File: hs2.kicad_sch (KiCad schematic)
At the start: 87 parts, among them J1 Conn_01x01, J2 Conn_01x01, J3 Conn_01x02, Q1 2N5457, Q2 2N3904, Q3 2N3906, Q4 2N3904, U1 Opamp_Dual, U2 Opamp_Dual, U3 Opamp_Dual

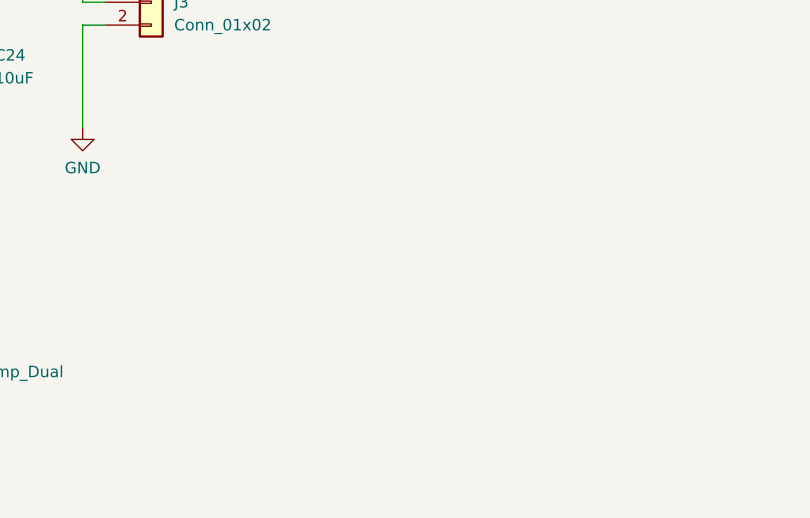
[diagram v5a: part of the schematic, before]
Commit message: schematics: Fixing ERC errors
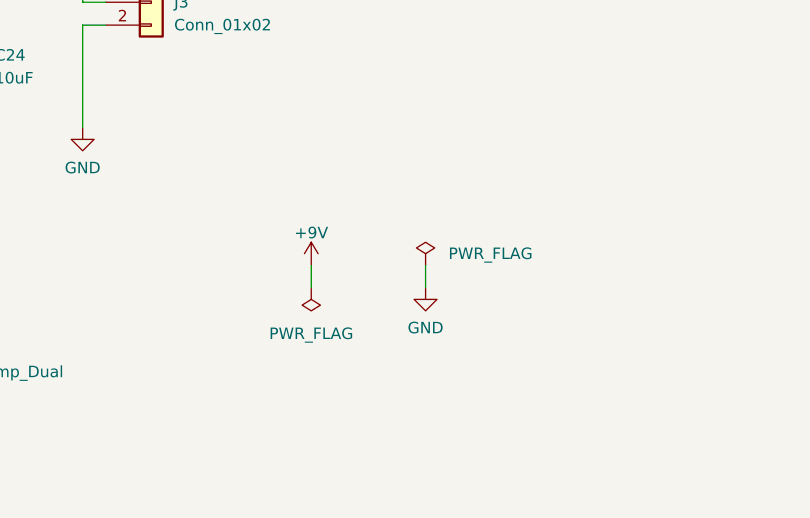
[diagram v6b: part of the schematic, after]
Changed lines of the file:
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@@
   (title_block
     (title "HS2")
-    (date "2022-08-09")
+    (date "2023-04-23")
     (rev "v1.0")
     (comment 1 "Author: Gabriel Mariano Marcelino <gabriel.mm8@gmail.com>")
@@
     (stroke (width 0) (type default) (color 0 0 0 0))
   )
+  (wire (pts (xy 114.3 215.9) (xy 114.3 218.44))
+    (stroke (width 0) (type default) (color 0 0 0 0))
+  )
   (wire (pts (xy 181.61 90.17) (xy 184.15 90.17))
     (stroke (width 0) (type default) (color 0 0 0 0))
@@
   )
   (wire (pts (xy 312.42 153.67) (xy 314.96 153.67))
+    (stroke (width 0) (type default) (color 0 0 0 0))
+  )
+  (wire (pts (xy 127 215.9) (xy 127 218.44))
     (stroke (width 0) (type default) (color 0 0 0 0))
   )
@@
     (pin "2")
   )
+  (symbol (lib_id "power:PWR_FLAG") (at 114.3 218.44 180) (unit 1)
+    (in_bom yes) (on_board yes) (fields_autoplaced)
+    (property "Reference" "#FLG0101" (id 0) (at 114.3 220.345 0)
+      (effects (font (size 1.27 1.27)) hide)
+    )
+    (property "Value" "PWR_FLAG" (id 1) (at 114.3 223.52 0))
+    (property "Footprint" "" (id 2) (at 114.3 218.44 0)
+      (effects (font (size 1.27 1.27)) hide)
+    )
+    (property "Datasheet" "~" (id 3) (at 114.3 218.44 0)
+      (effects (font (size 1.27 1.27)) hide)
+    )
+    (pin "1")
+  )
   (symbol (lib_id "Device:C") (at 302.26 181.61 0) (unit 1)
     (in_bom yes) (on_board yes) (fields_autoplaced)
@@
     (pin "1")
   )
+  (symbol (lib_id "power:+9V") (at 114.3 215.9 0) (unit 1)
+    (in_bom yes) (on_board yes) (fields_autoplaced)
+    (property "Reference" "#PWR0101" (id 0) (at 114.3 219.71 0)
+      (effects (font (size 1.27 1.27)) hide)
+    )
+    (property "Value" "+9V" (id 1) (at 114.3 212.3242 0))
+    (property "Footprint" "" (id 2) (at 114.3 215.9 0)
+      (effects (font (size 1.27 1.27)) hide)
+    )
+    (property "Datasheet" "" (id 3) (at 114.3 215.9 0)
+      (effects (font (size 1.27 1.27)) hide)
+    )
+    (pin "1")
+  )
   (symbol (lib_id "Mechanical:MountingHole_Pad") (at 356.87 27.94 0) (unit 1)
     (in_bom yes) (on_board yes) (fields_autoplaced)
@@
     (pin "2")
   )
+  (symbol (lib_id "power:PWR_FLAG") (at 127 215.9 0) (unit 1)
+    (in_bom yes) (on_board yes) (fields_autoplaced)
+    (property "Reference" "#FLG0102" (id 0) (at 127 213.995 0)
+      (effects (font (size 1.27 1.27)) hide)
+    )
+    (property "Value" "PWR_FLAG" (id 1) (at 129.54 214.6299 0)
+      (effects (font (size 1.27 1.27)) (justify left))
+    )
+    (property "Footprint" "" (id 2) (at 127 215.9 0)
+      (effects (font (size 1.27 1.27)) hide)
+    )
+    (property "Datasheet" "~" (id 3) (at 127 215.9 0)
+      (effects (font (size 1.27 1.27)) hide)
+    )
+    (pin "1")
+  )
   (symbol (lib_id "Device:C_Polarized") (at 76.2 194.31 0) (unit 1)
     (in_bom yes) (on_board yes) (fields_autoplaced)
@@
     (pin "8")
   )
+  (symbol (lib_id "power:GND") (at 127 218.44 0) (unit 1)
+    (in_bom yes) (on_board yes) (fields_autoplaced)
+    (property "Reference" "#PWR0102" (id 0) (at 127 224.79 0)
+      (effects (font (size 1.27 1.27)) hide)
+    )
+    (property "Value" "GND" (id 1) (at 127 222.8834 0))
+    (property "Footprint" "" (id 2) (at 127 218.44 0)
+      (effects (font (size 1.27 1.27)) hide)
+    )
+    (property "Datasheet" "" (id 3) (at 127 218.44 0)
+      (effects (font (size 1.27 1.27)) hide)
+    )
+    (pin "1")
+  )
   (symbol (lib_id "Device:Opamp_Dual") (at 40.64 226.06 0) (unit 3)
     (in_bom yes) (on_board yes) (fields_autoplaced)
@@
   )
   (symbol_instances
+    (path "/4c824f14-35f1-4cc5-99bb-3c6e3ad6c83a"
+      (reference "#FLG0101") (unit 1) (value "PWR_FLAG") (footprint "")
+    )
+    (path "/cedf0e6e-3270-4335-9e3d-b1ce42364208"
+      (reference "#FLG0102") (unit 1) (value "PWR_FLAG") (footprint "")
+    )
     (path "/16fc128f-9e86-4119-9573-3f9572c29789"
       (reference "#PWR01") (unit 1) (value "+9V") (footprint "")
@@
       (reference "#PWR029") (unit 1) (value "GND") (footprint "")
     )
+    (path "/8f56462a-9bae-4c7e-8266-0db49d616246"
+      (reference "#PWR0101") (unit 1) (value "+9V") (footprint "")
+    )
+    (path "/e58ef183-c306-4a6c-bc38-eb6d33dec87e"
+      (reference "#PWR0102") (unit 1) (value "GND") (footprint "")
+    )
     (path "/a51bbcfb-5528-4492-b6bc-f411b25693c0"

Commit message: Minor improvements
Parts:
- added J4, J5: Conn_01x01, Connector_PinHeader_2.54mm:PinHeader_1x01_P2.54mm_Vertical, symbol Connector_Generic:Conn_01x01
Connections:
- net +9V: now also J5.1 (Pin_1)
- net GND: now also J4.1 (Pin_1)
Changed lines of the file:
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@@
+    (stroke (width 0) (type default) (color 0 0 0 0))
+  )
+  (wire (pts (xy 29.21 113.03) (xy 29.21 115.57))
     (stroke (width 0) (type default) (color 0 0 0 0))
   )
@@
     (stroke (width 0) (type default) (color 0 0 0 0))
   )
+  (wire (pts (xy 127 175.26) (xy 127 177.8))
+    (stroke (width 0) (type default) (color 0 0 0 0))
+  )
   (wire (pts (xy 289.56 217.17) (xy 294.64 217.17))
     (stroke (width 0) (type default) (color 0 0 0 0))
@@
     (stroke (width 0) (type default) (color 0 0 0 0))
   )
+  (wire (pts (xy 26.67 113.03) (xy 29.21 113.03))
+    (stroke (width 0) (type default) (color 0 0 0 0))
+  )
   (wire (pts (xy 148.59 76.2) (xy 148.59 82.55))
     (stroke (width 0) (type default) (color 0 0 0 0))
@@
   )
   (wire (pts (xy 287.02 177.8) (xy 287.02 175.26))
+    (stroke (width 0) (type default) (color 0 0 0 0))
+  )
+  (wire (pts (xy 127 177.8) (xy 124.46 177.8))
     (stroke (width 0) (type default) (color 0 0 0 0))
   )
@@
     (pin "1")
     (pin "2")
+  )
+  (symbol (lib_id "Connector_Generic:Conn_01x01") (at 21.59 113.03 180) (unit 1)
+    (in_bom yes) (on_board yes) (fields_autoplaced)
+    (property "Reference" "J4" (id 0) (at 21.59 108.0602 0))
+    (property "Value" "Conn_01x01" (id 1) (at 21.59 110.5971 0))
+    (property "Footprint" "Connector_PinHeader_2.54mm:PinHeader_1x01_P2.54mm_Vertical" (id 2) (at 21.59 113.03 0)
+      (effects (font (size 1.27 1.27)) hide)
+    )
+    (property "Datasheet" "~" (id 3) (at 21.59 113.03 0)
+      (effects (font (size 1.27 1.27)) hide)
+    )
+    (pin "1")
   )
   (symbol (lib_id "Device:Opamp_Dual") (at 292.1 153.67 0) (mirror x) (unit 2)
@@
     (pin "2")
   )
+  (symbol (lib_id "power:+9V") (at 127 175.26 0) (unit 1)
+    (in_bom yes) (on_board yes) (fields_autoplaced)
+    (property "Reference" "#PWR031" (id 0) (at 127 179.07 0)
+      (effects (font (size 1.27 1.27)) hide)
+    )
+    (property "Value" "+9V" (id 1) (at 127 171.6842 0))
+    (property "Footprint" "" (id 2) (at 127 175.26 0)
+      (effects (font (size 1.27 1.27)) hide)
+    )
+    (property "Datasheet" "" (id 3) (at 127 175.26 0)
+      (effects (font (size 1.27 1.27)) hide)
+    )
+    (pin "1")
+  )
   (symbol (lib_id "power:GND") (at 88.9 200.66 0) (unit 1)
     (in_bom yes) (on_board yes) (fields_autoplaced)
@@
     )
     (property "Datasheet" "" (id 3) (at 88.9 200.66 0)
+      (effects (font (size 1.27 1.27)) hide)
+    )
+    (pin "1")
+  )
+  (symbol (lib_id "power:GND") (at 29.21 115.57 0) (unit 1)
+    (in_bom yes) (on_board yes) (fields_autoplaced)
+    (property "Reference" "#PWR030" (id 0) (at 29.21 121.92 0)
+      (effects (font (size 1.27 1.27)) hide)
+    )
+    (property "Value" "GND" (id 1) (at 29.21 120.0134 0))
+    (property "Footprint" "" (id 2) (at 29.21 115.57 0)
+      (effects (font (size 1.27 1.27)) hide)
+    )
+    (property "Datasheet" "" (id 3) (at 29.21 115.57 0)
       (effects (font (size 1.27 1.27)) hide)
     )
@@
     (pin "2")
   )
+  (symbol (lib_id "Connector_Generic:Conn_01x01") (at 119.38 177.8 180) (unit 1)
+    (in_bom yes) (on_board yes) (fields_autoplaced)
+    (property "Reference" "J5" (id 0) (at 119.38 172.8302 0))
+    (property "Value" "Conn_01x01" (id 1) (at 119.38 175.3671 0))
+    (property "Footprint" "Connector_PinHeader_2.54mm:PinHeader_1x01_P2.54mm_Vertical" (id 2) (at 119.38 177.8 0)
+      (effects (font (size 1.27 1.27)) hide)
+    )
+    (property "Datasheet" "~" (id 3) (at 119.38 177.8 0)
+      (effects (font (size 1.27 1.27)) hide)
+    )
+    (pin "1")
+  )
   (symbol (lib_id "Device:Opamp_Dual") (at 59.69 226.06 0) (unit 3)
     (in_bom yes) (on_board yes) (fields_autoplaced)
@@
       (reference "#PWR029") (unit 1) (value "GND") (footprint "")
     )
+    (path "/40b66e0c-1dc0-43a7-ac39-2ab51f367b7d"
+      (reference "#PWR030") (unit 1) (value "GND") (footprint "")
+    )
+    (path "/3c09fc08-7353-4b6a-b6bb-0c1a96258f69"
+      (reference "#PWR031") (unit 1) (value "+9V") (footprint "")
+    )
     (path "/8f56462a-9bae-4c7e-8266-0db49d616246"
       (reference "#PWR0101") (unit 1) (value "+9V") (footprint "")
@@
       (reference "J3") (unit 1) (value "Conn_01x02") (footprint "Connector_PinHeader_2.54mm:PinHeader_1x02_P2.54mm_Vertical")
     )
+    (path "/0923cfc4-bd5e-4cab-b9fb-6414e070667a"
+      (reference "J4") (unit 1) (value "Conn_01x01") (footprint "Connector_PinHeader_2.54mm:PinHeader_1x01_P2.54mm_Vertical")
+    )
+    (path "/eec560e0-c62a-4c20-9f6f-6af2f79b49af"
+      (reference "J5") (unit 1) (value "Conn_01x01") (footprint "Connector_PinHeader_2.54mm:PinHeader_1x01_P2.54mm_Vertical")
+    )
     (path "/4a29da74-715d-4689-ad8d-94ecf2cd25fe"
